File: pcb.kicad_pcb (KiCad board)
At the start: 2 copper layers, 76 parts, among them SW1 SW_Push, U1 ATmega32U4-AU, Y1 16MHz

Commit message: Updated PCB from Schematic
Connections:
- U1 pad 28: ROW4 -> Net-(U1-Pad28)
- U1 pad 29: ROW3 -> Net-(U1-Pad29)
- U1 pad 30: ROW2 -> Net-(U1-Pad30)
- U1 pad 31: ROW1 -> Net-(U1-Pad31)
- U1 pad 32: ROW0 -> Net-(U1-Pad32)
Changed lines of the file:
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@@
     (zones 0)
     (modules 76)
-    (nets 77)
+    (nets 82)
   )
   (page A4)
@@
   (net 59 "Net-(U1-Pad37)")
   (net 60 "Net-(U1-Pad36)")
-  (net 61 "Net-(U1-Pad27)")
-  (net 62 "Net-(U1-Pad26)")
-  (net 63 "Net-(U1-Pad22)")
-  (net 64 "Net-(U1-Pad12)")
-  (net 65 "Net-(U1-Pad1)")
-  (net 66 "Net-(USB1-Pad6)")
-  (net 67 "Net-(USB1-Pad2)")
-  (net 68 "Net-(U1-Pad25)")
-  (net 69 "Net-(U1-Pad11)")
-  (net 70 "Net-(U1-Pad10)")
-  (net 71 "Net-(U1-Pad9)")
-  (net 72 "Net-(U1-Pad8)")
-  (net 73 "Net-(U1-Pad21)")
-  (net 74 "Net-(U1-Pad20)")
-  (net 75 "Net-(U1-Pad19)")
-  (net 76 "Net-(U1-Pad18)")
+  (net 61 "Net-(U1-Pad32)")
+  (net 62 "Net-(U1-Pad31)")
+  (net 63 "Net-(U1-Pad30)")
+  (net 64 "Net-(U1-Pad27)")
+  (net 65 "Net-(U1-Pad26)")
+  (net 66 "Net-(U1-Pad22)")
+  (net 67 "Net-(U1-Pad12)")
+  (net 68 "Net-(U1-Pad1)")
+  (net 69 "Net-(USB1-Pad6)")
+  (net 70 "Net-(USB1-Pad2)")
+  (net 71 "Net-(U1-Pad25)")
+  (net 72 "Net-(U1-Pad29)")
+  (net 73 "Net-(U1-Pad28)")
+  (net 74 "Net-(U1-Pad11)")
+  (net 75 "Net-(U1-Pad10)")
+  (net 76 "Net-(U1-Pad9)")
+  (net 77 "Net-(U1-Pad8)")
+  (net 78 "Net-(U1-Pad21)")
+  (net 79 "Net-(U1-Pad20)")
+  (net 80 "Net-(U1-Pad19)")
+  (net 81 "Net-(U1-Pad18)")
   (net_class Default "This is the default net class."
     (clearance 0.2)
@@
     (add_net "Net-(U1-Pad26)")
     (add_net "Net-(U1-Pad27)")
+    (add_net "Net-(U1-Pad28)")
+    (add_net "Net-(U1-Pad29)")
+    (add_net "Net-(U1-Pad30)")
+    (add_net "Net-(U1-Pad31)")
+    (add_net "Net-(U1-Pad32)")
     (add_net "Net-(U1-Pad36)")
     (add_net "Net-(U1-Pad37)")
@@
     (fp_line (start -3.75 -3.85) (end -3.75 3.85) (layer Dwgs.User) (width 0.15))
     (pad 6 thru_hole oval (at 0 -3.65 270) (size 2.7 1.7) (drill oval 1.9 0.7) (layers *.Cu *.Mask)
-      (net 66 "Net-(USB1-Pad6)"))
+      (net 69 "Net-(USB1-Pad6)"))
     (pad 6 thru_hole oval (at 0 3.65 270) (size 2.7 1.7) (drill oval 1.9 0.7) (layers *.Cu *.Mask)
-      (net 66 "Net-(USB1-Pad6)"))
+      (net 69 "Net-(USB1-Pad6)"))
     (pad 6 thru_hole oval (at 4.5 3.65 270) (size 2.7 1.7) (drill oval 1.9 0.7) (layers *.Cu *.Mask)
-      (net 66 "Net-(USB1-Pad6)"))
+      (net 69 "Net-(USB1-Pad6)"))
     (pad 6 thru_hole oval (at 4.5 -3.65 270) (size 2.7 1.7) (drill oval 1.9 0.7) (layers *.Cu *.Mask)
-      (net 66 "Net-(USB1-Pad6)"))
+      (net 69 "Net-(USB1-Pad6)"))
     (pad 5 smd rect (at 4.5 -1.6 270) (size 2.25 0.5) (layers F.Cu F.Paste F.Mask)
       (net 41 VCC))
@@
       (net 48 D+))
     (pad 2 smd rect (at 4.5 0.8 270) (size 2.25 0.5) (layers F.Cu F.Paste F.Mask)
-      (net 67 "Net-(USB1-Pad2)"))
+      (net 70 "Net-(USB1-Pad2)"))
     (pad 1 smd rect (at 4.5 1.6 270) (size 2.25 0.5) (layers F.Cu F.Paste F.Mask)
       (net 1 GND))
@@
       (net 53 "Net-(R4-Pad2)"))
     (pad 32 smd rect (at 5.7 -3.2 270) (size 1.5 0.55) (layers F.Cu F.Paste F.Mask)
-      (net 15 ROW0))
+      (net 61 "Net-(U1-Pad32)"))
     (pad 31 smd rect (at 5.7 -2.4 270) (size 1.5 0.55) (layers F.Cu F.Paste F.Mask)
-      (net 13 ROW1))
+      (net 62 "Net-(U1-Pad31)"))
     (pad 30 smd rect (at 5.7 -1.6 270) (size 1.5 0.55) (layers F.Cu F.Paste F.Mask)
-      (net 11 ROW2))
+      (net 63 "Net-(U1-Pad30)"))
     (pad 29 smd rect (at 5.7 -0.8 270) (size 1.5 0.55) (layers F.Cu F.Paste F.Mask)
-      (net 9 ROW3))
+      (net 72 "Net-(U1-Pad29)"))
     (pad 28 smd rect (at 5.7 0 270) (size 1.5 0.55) (layers F.Cu F.Paste F.Mask)
-      (net 7 ROW4))
+      (net 73 "Net-(U1-Pad28)"))
     (pad 27 smd rect (at 5.7 0.8 270) (size 1.5 0.55) (layers F.Cu F.Paste F.Mask)
-      (net 61 "Net-(U1-Pad27)"))
+      (net 64 "Net-(U1-Pad27)"))
     (pad 26 smd rect (at 5.7 1.6 270) (size 1.5 0.55) (layers F.Cu F.Paste F.Mask)
-      (net 62 "Net-(U1-Pad26)"))
+      (net 65 "Net-(U1-Pad26)"))
     (pad 25 smd rect (at 5.7 2.4 270) (size 1.5 0.55) (layers F.Cu F.Paste F.Mask)
-      (net 68 "Net-(U1-Pad25)"))
+      (net 71 "Net-(U1-Pad25)"))
     (pad 24 smd rect (at 5.7 3.2 270) (size 1.5 0.55) (layers F.Cu F.Paste F.Mask)
       (net 2 +5V))
@@
       (net 1 GND))
     (pad 22 smd rect (at 4 5.7) (size 1.5 0.55) (layers F.Cu F.Paste F.Mask)
-      (net 63 "Net-(U1-Pad22)"))
+      (net 66 "Net-(U1-Pad22)"))
     (pad 21 smd rect (at 3.2 5.7) (size 1.5 0.55) (layers F.Cu F.Paste F.Mask)
-      (net 73 "Net-(U1-Pad21)"))
+      (net 78 "Net-(U1-Pad21)"))
     (pad 20 smd rect (at 2.4 5.7) (size 1.5 0.55) (layers F.Cu F.Paste F.Mask)
-      (net 74 "Net-(U1-Pad20)"))
+      (net 79 "Net-(U1-Pad20)"))
     (pad 19 smd rect (at 1.6 5.7) (size 1.5 0.55) (layers F.Cu F.Paste F.Mask)
-      (net 75 "Net-(U1-Pad19)"))
+      (net 80 "Net-(U1-Pad19)"))
     (pad 18 smd rect (at 0.8 5.7) (size 1.5 0.55) (layers F.Cu F.Paste F.Mask)
-      (net 76 "Net-(U1-Pad18)"))
+      (net 81 "Net-(U1-Pad18)"))
     (pad 17 smd rect (at 0 5.7) (size 1.5 0.55) (layers F.Cu F.Paste F.Mask)
       (net 3 "Net-(C4-Pad1)"))
@@
       (net 52 "Net-(R3-Pad2)"))
     (pad 12 smd rect (at -4 5.7) (size 1.5 0.55) (layers F.Cu F.Paste F.Mask)
-      (net 64 "Net-(U1-Pad12)"))
+      (net 67 "Net-(U1-Pad12)"))
     (pad 11 smd rect (at -5.7 4 270) (size 1.5 0.55) (layers F.Cu F.Paste F.Mask)
-      (net 69 "Net-(U1-Pad11)"))
+      (net 74 "Net-(U1-Pad11)"))
     (pad 10 smd rect (at -5.7 3.2 270) (size 1.5 0.55) (layers F.Cu F.Paste F.Mask)
-      (net 70 "Net-(U1-Pad10)"))
+      (net 75 "Net-(U1-Pad10)"))
     (pad 9 smd rect (at -5.7 2.4 270) (size 1.5 0.55) (layers F.Cu F.Paste F.Mask)
-      (net 71 "Net-(U1-Pad9)"))
+      (net 76 "Net-(U1-Pad9)"))
     (pad 8 smd rect (at -5.7 1.6 270) (size 1.5 0.55) (layers F.Cu F.Paste F.Mask)
-      (net 72 "Net-(U1-Pad8)"))
+      (net 77 "Net-(U1-Pad8)"))
     (pad 7 smd rect (at -5.7 0.8 270) (size 1.5 0.55) (layers F.Cu F.Paste F.Mask)
       (net 2 +5V))
@@
       (net 2 +5V))
     (pad 1 smd rect (at -5.7 -4 270) (size 1.5 0.55) (layers F.Cu F.Paste F.Mask)
-      (net 65 "Net-(U1-Pad1)"))
+      (net 68 "Net-(U1-Pad1)"))
     (model ${KISYS3DMOD}/Package_QFP.3dshapes/TQFP-44_10x10mm_P0.8mm.wrl
       (at (xyz 0 0 0))

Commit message: Made Changes
idk
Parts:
- MX1, MX10, MX11, MX12, MX13, MX14, MX15, MX16, MX17, MX18, MX19, MX20, MX22, MX23, MX24, MX25, MX26, MX27, MX28, MX29, MX30, MX5, MX6, MX7, MX8, MX9: footprint MX_Alps_Hybrid_Included:MX-1U -> MX_Alps_Hybrid_Included:MX-1U-NoLED
- MX2, MX21: footprint MX_Alps_Hybrid_Included:MX-1U -> MX_Alps_Hybrid_Included:MX-2U-NoLED
- MX3: footprint MX_Alps_Hybrid_Included:MX-1U -> MX_Alps_Hybrid_Included:MX-1.75U-NoLED
- MX4: footprint MX_Alps_Hybrid_Included:MX-1U -> MX_Alps_Hybrid_Included:MX-1.5U-NoLED
- moved D15 271.5 mm to (111.0, 36.6), turned to 180 degrees
- moved D20 271.1 mm to (129.8, 36.6), turned to 180 degrees
- moved D25 271.1 mm to (148.8, 36.6), turned to 180 degrees
- moved D1 271.0 mm to (72.9, 112.8), turned to 180 degrees
- moved MX25 271.0 mm to (149.6, 42.4), turned to 180 degrees
- moved MX1 271.0 mm to (73.4, 118.6), turned to 180 degrees
- moved MX10 271.0 mm to (92.5, 42.4), turned to 180 degrees
- moved MX11 271.0 mm to (111.5, 118.6), turned to 180 degrees
- moved MX15 271.0 mm to (111.5, 42.4), turned to 180 degrees
- moved MX16 271.0 mm to (130.6, 118.6), turned to 180 degrees
- moved MX20 271.0 mm to (130.6, 42.4), turned to 180 degrees
- moved MX30 271.0 mm to (168.7, 42.4), turned to 180 degrees
- moved MX5 271.0 mm to (73.4, 42.4), turned to 180 degrees
- moved MX6 271.0 mm to (92.5, 118.6), turned to 180 degrees
- moved D6 270.8 mm to (92.2, 112.8), turned to 180 degrees
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
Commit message: No idea
No clue what's changed
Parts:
- C1, C2, C3, C4, C5, C6, C7, F1, R1, R2, R3, R4, SW1, U1, USB1, Y1: moved to B.Cu
- D1, D10, D11, D12, D13, D14, D15, D16, D17, D18, D19, D2, D20, D21, D22, D23, D24, D25, D26, D27, D28, D29, D3, D30, D4, D5, D6, D7, D8, D9: moved to F.Cu
- moved SW1 329.1 mm to (24.9, 116.0), turned to 90 degrees
- moved C1 319.5 mm to (24.0, 150.9), turned to 0 degrees
- moved C2 317.9 mm to (23.9, 146.0), turned to 0 degrees
- moved C3 316.4 mm to (24.0, 141.1), turned to 0 degrees
- moved C7 315.1 mm to (24.0, 136.2), turned to 0 degrees
- moved USB1 286.2 mm to (142.1, 91.3)
- moved R1 284.1 mm to (150.0, 105.4), turned to 90 degrees
- moved R2 280.4 mm to (152.4, 105.4), turned to 90 degrees
- moved F1 279.9 mm to (148.6, 100.8), turned to 180 degrees
- moved C6 279.4 mm to (147.6, 105.4), turned to 90 degrees
- moved U1 276.4 mm to (149.6, 115.3), turned to 90 degrees
- moved R3 269.9 mm to (138.3, 101.6)
- moved C4 269.5 mm to (138.3, 106.8), turned to 0 degrees
- moved Y1 265.4 mm to (143.1, 105.4), turned to 90 degrees
- moved R4 263.2 mm to (152.4, 101.6), turned to 90 degrees
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
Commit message: Attempt 1
Attempt 1
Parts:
- moved USB1 0.16 mm to (142.2, 91.3)
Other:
- net class Default removed

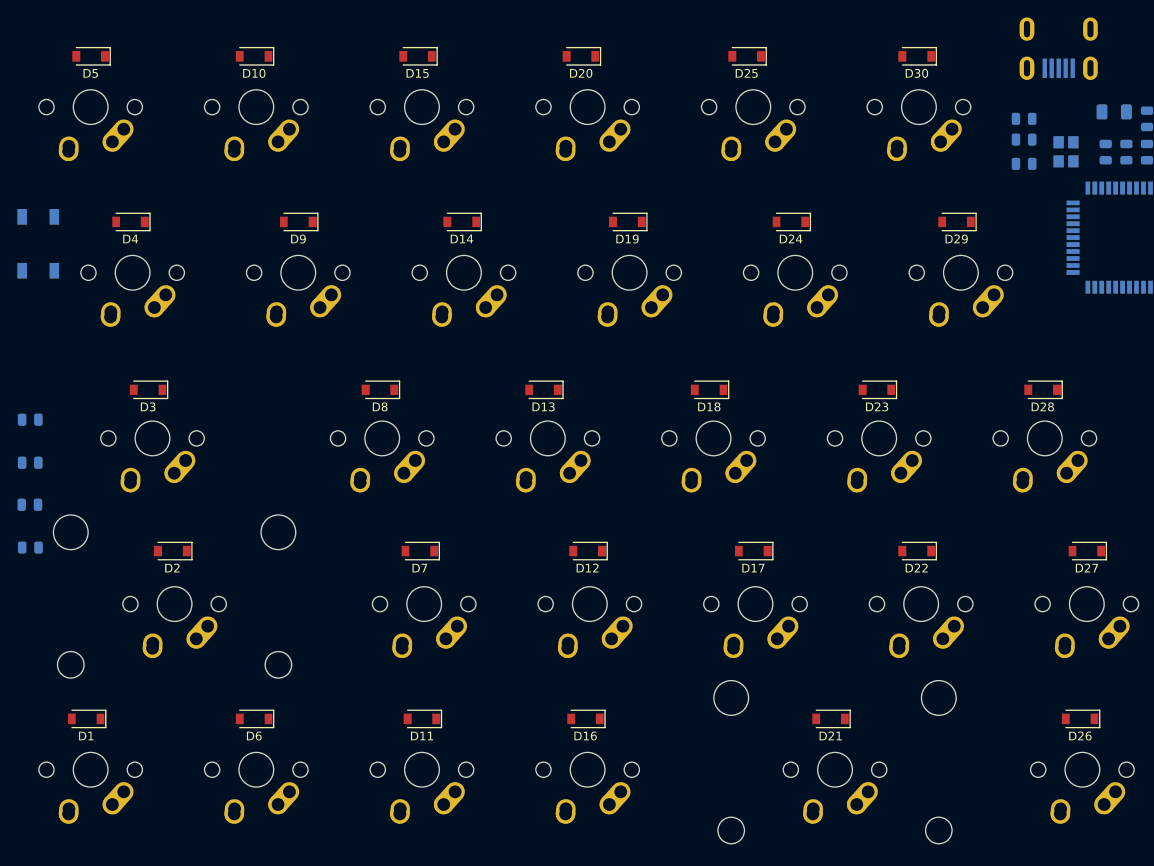
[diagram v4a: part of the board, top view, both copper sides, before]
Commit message: Tracing
Traces for diodes done. Switch traces started
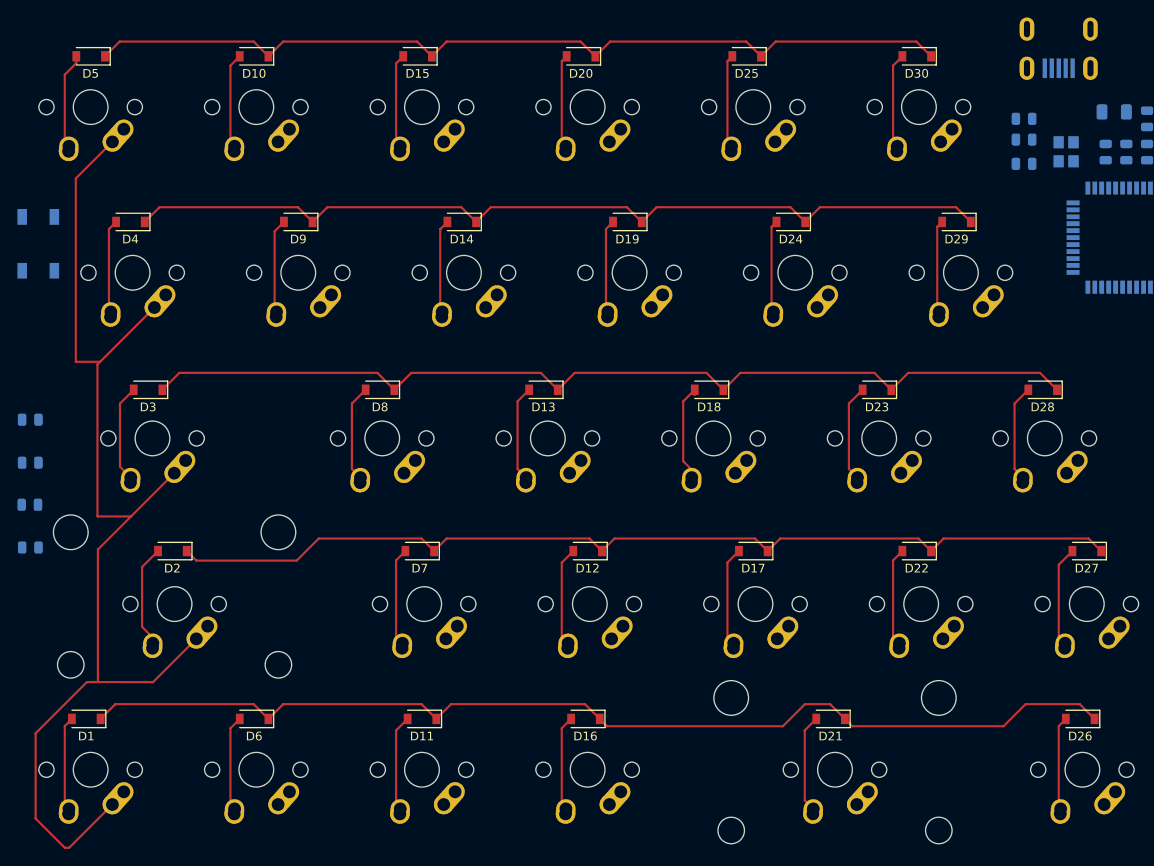
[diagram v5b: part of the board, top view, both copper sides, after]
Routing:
- net COL0: track 0.00 -> 136.6 mm
- net ROW4: track 0.00 -> 122.7 mm
- net ROW3: track 0.00 -> 112.0 mm
- net ROW2: track 0.00 -> 110.9 mm
- net ROW0: track 0.00 -> 102.0 mm
- net ROW1: track 0.00 -> 102.0 mm
- net Net-(D27-Pad2): track 0.00 -> 11.6 mm
- net Net-(D17-Pad2): track 0.00 -> 11.4 mm
- net Net-(D12-Pad2): track 0.00 -> 11.4 mm
- net Net-(D22-Pad2): track 0.00 -> 11.3 mm
- net Net-(D7-Pad2): track 0.00 -> 11.3 mm
- net Net-(D21-Pad2): track 0.00 -> 11.3 mm
- net Net-(D2-Pad2): track 0.00 -> 11.3 mm
- net Net-(D3-Pad2): track 0.00 -> 11.3 mm
- net Net-(D18-Pad2): track 0.00 -> 11.2 mm
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
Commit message: Routing Cont
Routing between switches and diodes v0.1 done
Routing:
- net COL3: track 0.00 -> 90.5 mm
- net COL2: track 0.00 -> 89.5 mm
- net COL1: track 0.00 -> 88.6 mm
- net COL4: track 0.00 -> 84.5 mm
- net COL5: track 0.00 -> 80.3 mm
- net COL0: track 136.6 -> 83.6 mm
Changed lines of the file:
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@@
   (segment (start 123.19 95.478) (end 123.19 104.14) (width 0.25) (layer "F.Cu") (net 40))
   (segment (start 124.262 94.406) (end 123.19 95.478) (width 0.25) (layer "F.Cu") (net 40))
-  (segment (start 35.558 147.318) (end 31.75 151.126) (width 0.25) (layer "F.Cu") (net 42))
-  (segment (start 33.416 180.448) (end 28.444 185.42) (width 0.25) (layer "F.Cu") (net 42))
-  (segment (start 32 129.54) (end 38.242 123.298) (width 0.25) (layer "F.Cu") (net 42))
-  (segment (start 32 129.54) (end 31.697999 129.842001) (width 0.25) (layer "F.Cu") (net 42))
-  (segment (start 31.75 166.37) (end 38.096 166.37) (width 0.25) (layer "F.Cu") (net 42))
-  (segment (start 38.096 166.37) (end 34.594 166.37) (width 0.25) (layer "F.Cu") (net 42))
-  (segment (start 29.21 129.54) (end 32 129.54) (width 0.25) (layer "F.Cu") (net 42))
-  (segment (start 24.585999 182.065999) (end 24.585999 172.264001) (width 0.25) (layer "F.Cu") (net 42))
-  (segment (start 38.096 166.37) (end 43.068 161.398) (width 0.25) (layer "F.Cu") (net 42))
-  (segment (start 27.94 185.42) (end 24.585999 182.065999) (width 0.25) (layer "F.Cu") (net 42))
-  (segment (start 30.48 166.37) (end 31.75 166.37) (width 0.25) (layer "F.Cu") (net 42))
-  (segment (start 28.444 185.42) (end 27.94 185.42) (width 0.25) (layer "F.Cu") (net 42))
-  (segment (start 35.556 147.32) (end 35.558 147.318) (width 0.25) (layer "F.Cu") (net 42))
-  (segment (start 24.585999 172.264001) (end 30.48 166.37) (width 0.25) (layer "F.Cu") (net 42))
-  (segment (start 29.21 108.454) (end 29.21 129.54) (width 0.25) (layer "F.Cu") (net 42))
-  (segment (start 33.416 104.248) (end 29.21 108.454) (width 0.25) (layer "F.Cu") (net 42))
-  (segment (start 34.745999 178.968001) (end 34.726 178.988) (width 0.25) (layer "F.Cu") (net 42))
-  (segment (start 31.75 147.32) (end 35.556 147.32) (width 0.25) (layer "F.Cu") (net 42))
-  (segment (start 31.697999 129.842001) (end 31.697999 147.267999) (width 0.25) (layer "F.Cu") (net 42))
-  (segment (start 35.558 147.318) (end 40.528 142.348) (width 0.25) (layer "F.Cu") (net 42))
-  (segment (start 31.75 151.126) (end 31.75 166.37) (width 0.25) (layer "F.Cu") (net 42))
-  (segment (start 31.697999 147.267999) (end 31.75 147.32) (width 0.25) (layer "F.Cu") (net 42))
+  (segment (start 44.378 159.938) (end 44.378 169.833769) (width 0.25) (layer "B.Cu") (net 42))
+  (segment (start 44.378 169.833769) (end 35.223769 178.988) (width 0.25) (layer "B.Cu") (net 42))
+  (segment (start 35.223769 178.988) (end 34.726 178.988) (width 0.25) (layer "B.Cu") (net 42))
+  (segment (start 39.552 121.838) (end 41.838 124.124) (width 0.25) (layer "B.Cu") (net 42))
+  (segment (start 44.378 143.428) (end 44.378 159.938) (width 0.25) (layer "B.Cu") (net 42))
+  (segment (start 39.552 110.384) (end 39.552 121.838) (width 0.25) (layer "B.Cu") (net 42))
+  (segment (start 41.838 124.124) (end 41.838 140.888) (width 0.25) (layer "B.Cu") (net 42))
+  (segment (start 41.838 140.888) (end 44.378 143.428) (width 0.25) (layer "B.Cu") (net 42))
+  (segment (start 33.416 104.248) (end 39.552 110.384) (width 0.25) (layer "B.Cu") (net 42))
+  (segment (start 52.466 104.248) (end 58.621999 110.403999) (width 0.25) (layer "B.Cu") (net 43))
+  (segment (start 57.292 123.298) (end 68.254 134.26) (width 0.25) (layer "B.Cu") (net 43))
+  (segment (start 55.77099 178.988) (end 53.776 178.988) (width 0.25) (layer "B.Cu") (net 43))
+  (segment (start 71.77 161.398) (end 71.77 162.98899) (width 0.25) (layer "B.Cu") (net 43))
+  (segment (start 58.621999 121.818001) (end 58.602 121.838) (width 0.25) (layer "B.Cu") (net 43))
+  (segment (start 73.08 148.484) (end 73.08 159.938) (width 0.25) (layer "B.Cu") (net 43))
+  (segment (start 66.944 142.348) (end 73.08 148.484) (width 0.25) (layer "B.Cu") (net 43))
+  (segment (start 68.254 134.26) (end 68.254 140.888) (width 0.25) (layer "B.Cu") (net 43))
+  (segment (start 58.621999 110.403999) (end 58.621999 121.818001) (width 0.25) (layer "B.Cu") (net 43))
+  (segment (start 71.77 162.98899) (end 55.77099 178.988) (width 0.25) (layer "B.Cu") (net 43))
+  (segment (start 74.786231 173.99) (end 72.826 175.950231) (width 0.25) (layer "B.Cu") (net 44))
+  (segment (start 85.994 142.348) (end 92.13 148.484) (width 0.25) (layer "B.Cu") (net 44))
+  (segment (start 76.342 123.298) (end 87.304 134.26) (width 0.25) (layer "B.Cu") (net 44))
+  (segment (start 90.82 161.398) (end 78.228 173.99) (width 0.25) (layer "B.Cu") (net 44))
+  (segment (start 72.826 175.950231) (end 72.826 178.988) (width 0.25) (layer "B.Cu") (net 44))
+  (segment (start 92.13 148.484) (end 92.13 159.938) (width 0.25) (layer "B.Cu") (net 44))
+  (segment (start 78.228 173.99) (end 74.786231 173.99) (width 0.25) (layer "B.Cu") (net 44))
+  (segment (start 77.652 110.384) (end 77.652 121.838) (width 0.25) (layer "B.Cu") (net 44))
+  (segment (start 87.304 134.26) (end 87.304 140.888) (width 0.25) (layer "B.Cu") (net 44))
+  (segment (start 71.516 104.248) (end 77.652 110.384) (width 0.25) (layer "B.Cu") (net 44))
+  (segment (start 97.131133 178.988) (end 91.876 178.988) (width 0.25) (layer "B.Cu") (net 45))
+  (segment (start 105.044 142.348) (end 111.18 148.484) (width 0.25) (layer "B.Cu") (net 45))
+  (segment (start 96.702 110.384) (end 96.702 121.838) (width 0.25) (layer "B.Cu") (net 45))
+  (segment (start 109.87 166.249133) (end 97.131133 178.988) (width 0.25) (layer "B.Cu") (net 45))
+  (segment (start 111.18 148.484) (end 111.18 159.938) (width 0.25) (layer "B.Cu") (net 45))
+  (segment (start 106.354 134.26) (end 106.354 140.888) (width 0.25) (layer "B.Cu") (net 45))
+  (segment (start 109.87 161.398) (end 109.87 166.249133) (width 0.25) (layer "B.Cu") (net 45))
+  (segment (start 95.392 123.298) (end 106.354 134.26) (width 0.25) (layer "B.Cu") (net 45))
+  (segment (start 90.566 104.248) (end 96.702 110.384) (width 0.25) (layer "B.Cu") (net 45))
+  (segment (start 124.094 142.348) (end 130.23 148.484) (width 0.25) (layer "B.Cu") (net 46))
+  (segment (start 130.23 148.484) (end 130.23 159.938) (width 0.25) (layer "B.Cu") (net 46))
+  (segment (start 123.19 177.8) (end 122.002 178.988) (width 0.25) (layer "B.Cu") (net 46))
+  (segment (start 109.616 104.248) (end 115.752 110.384) (width 0.25) (layer "B.Cu") (net 46))
+  (segment (start 125.404 134.26) (end 125.404 140.888) (width 0.25) (layer "B.Cu") (net 46))
+  (segment (start 114.442 123.298) (end 125.404 134.26) (width 0.25) (layer "B.Cu") (net 46))
+  (segment (start 122.002 178.988) (end 120.324 178.988) (width 0.25) (layer "B.Cu") (net 46))
+  (segment (start 123.19 167.128) (end 123.19 177.8) (width 0.25) (layer "B.Cu") (net 46))
+  (segment (start 115.752 110.384) (end 115.752 121.838) (width 0.25) (layer "B.Cu") (net 46))
+  (segment (start 128.92 161.398) (end 123.19 167.128) (width 0.25) (layer "B.Cu") (net 46))
+  (segment (start 144.454 134.26) (end 144.454 140.888) (width 0.25) (layer "B.Cu") (net 47))
+  (segment (start 134.821999 121.818001) (end 134.802 121.838) (width 0.25) (layer "B.Cu") (net 47))
+  (segment (start 147.97 178.186) (end 148.772 178.988) (width 0.25) (layer "B.Cu") (net 47))
+  (segment (start 134.821999 110.403999) (end 134.821999 121.818001) (width 0.25) (layer "B.Cu") (net 47))
+  (segment (start 147.97 161.398) (end 147.97 178.186) (width 0.25) (layer "B.Cu") (net 47))
+  (segment (start 149.28 148.484) (end 149.28 159.938) (width 0.25) (layer "B.Cu") (net 47))
+  (segment (start 143.144 142.348) (end 149.28 148.484) (width 0.25) (layer "B.Cu") (net 47))
+  (segment (start 128.666 104.248) (end 134.821999 110.403999) (width 0.25) (layer "B.Cu") (net 47))
+  (segment (start 133.492 123.298) (end 144.454 134.26) (width 0.25) (layer "B.Cu") (net 47))
 )
